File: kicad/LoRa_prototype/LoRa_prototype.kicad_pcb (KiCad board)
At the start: 2 copper layers, 145 parts, among them J1 Conn_ST_STDC14, J10 SYS, J11 BME, J12 GPS, J13 GPS_UART, J14 SPI_FLASH, J15 SYS, J18 MCO, J2 USB_C_Receptacle_PowerOnly_6P, J3 BAT, J4 SMA Female, J5 FG, J6 I2C1, J7 BQ, J8 BMV, J9 UART1, Q1 DTC143Z, Q2 DTC143Z, SW1 NRST, U1 TC1262-33, U10 STM32WL54CCUx, U2 BQ24074RGTT, U3 MAX17048, U4 SPV1050, U5 AS179-92LF, U6 L80-R, U7 BME688, U8 W25Q16JVSS, U9 BMV080, X1 LSE, X2 NT2016SF

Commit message: Routed HSE
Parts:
- removed R2: 0, Resistor_SMD:R_0603_1608Metric
- moved X2 81.9 mm to (157.7, 103.0)
- moved X1 69.2 mm to (175.2, 106.0)
- moved C9 54.2 mm to (157.8, 105.5), turned to 180 degrees
- moved C4 52.5 mm to (174.4, 104.0)
- moved C8 52.0 mm to (174.4, 108.0)
- moved C2 51.8 mm to (157.8, 100.5)
- moved C10 33.8 mm to (68.5, 155.8)
- moved C35 33.8 mm to (61.1, 154.6)
- moved C36 33.8 mm to (61.1, 157.7)
- moved C7 33.8 mm to (68.5, 154.0)
- moved J4 33.8 mm to (62.2, 148.6)
- moved C37 33.8 mm to (61.1, 160.7)
- moved L8 33.8 mm to (65.3, 154.4)
- moved U5 33.8 mm to (65.3, 160.0)
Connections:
- C7 pad 1: Net-(C7-Pad1) -> Net-(C37-Pad2)
- L8 pad 1: Net-(C7-Pad1) -> Net-(C37-Pad2)
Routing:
- net Net-(X2-OUT): track 0.00 -> 5.53 mm
- net /MCU/VDD_TCXO: track 0.00 -> 4.85 mm
- net /MCU/HSE32_IN: track 0.00 -> 3.44 mm
- net GND: track 0.00 -> 1.80 mm

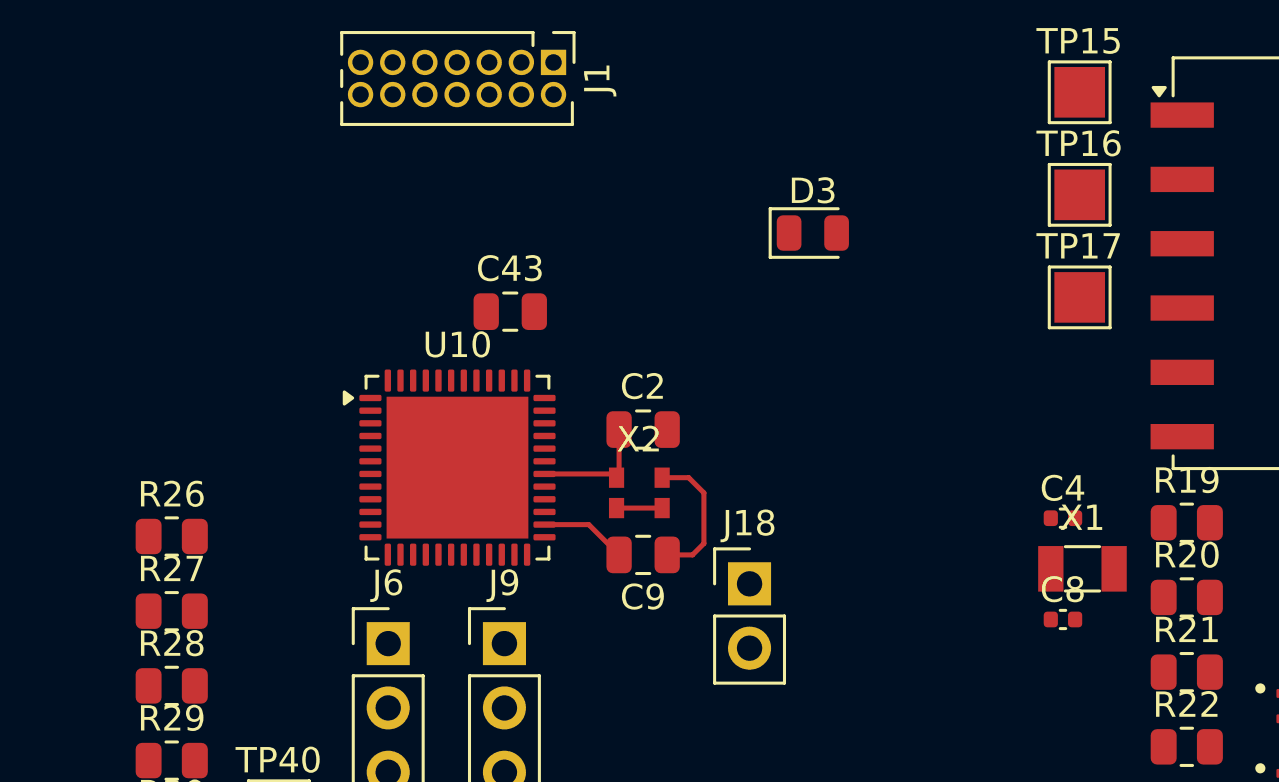
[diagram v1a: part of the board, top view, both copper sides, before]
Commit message: Routed LSE
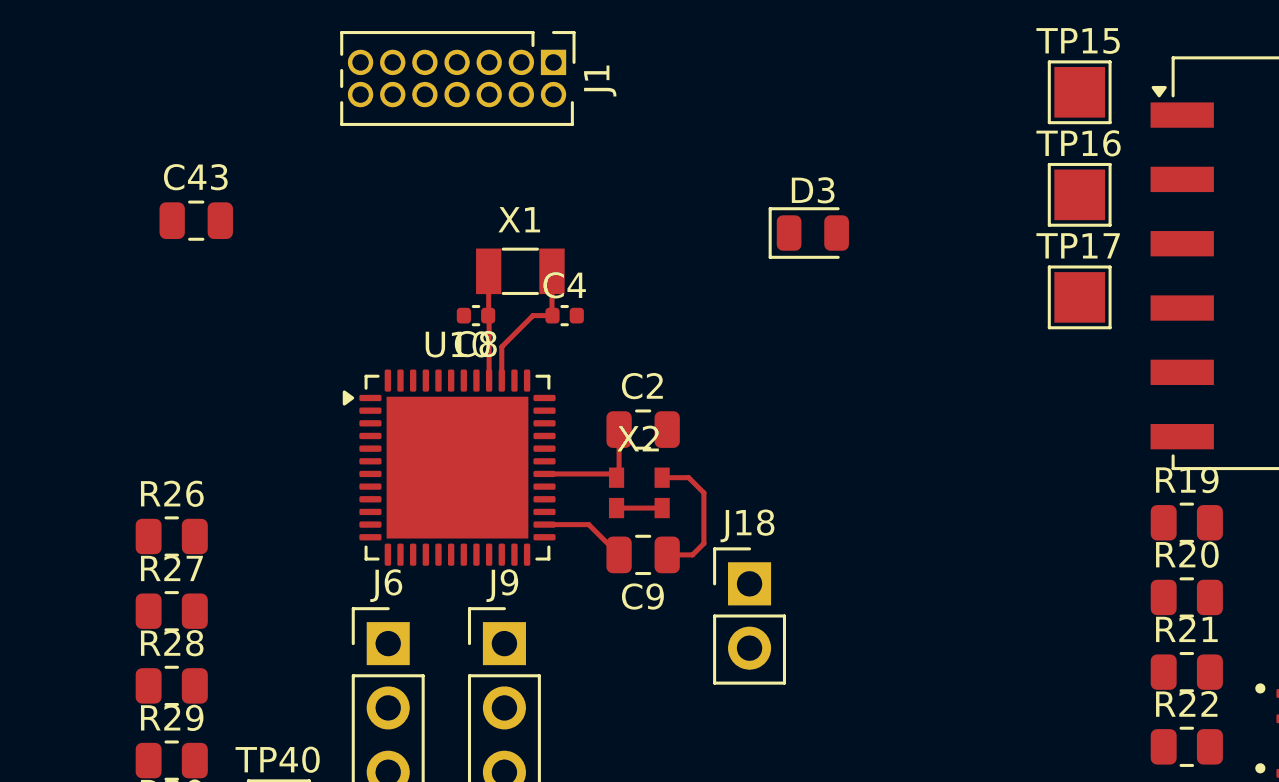
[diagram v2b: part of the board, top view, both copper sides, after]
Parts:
- moved C8 26.1 mm to (151.2, 96.0), turned to 180 degrees
- moved X1 25.1 mm to (153.0, 94.2)
- moved C4 21.2 mm to (154.8, 96.0)
- moved C43 12.9 mm to (140.2, 92.2)
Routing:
- net /MCU/OSC32_IN: track 0.00 -> 5.60 mm
- net /MCU/OSC32_OUT: track 0.00 -> 4.34 mm
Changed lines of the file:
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@@
 	(footprint "Capacitor_SMD:C_0402_1005Metric"
 		(layer "F.Cu")
-		(at 174.43 104)
+		(at 154.75 96)
 		(descr "Capacitor SMD 0402 (1005 Metric), square (rectangular) end terminal, IPC-7351 nominal, (Body size source: IPC-SM-782 page 76, https://www.pcb-3d.com/wordpress/wp-content/uploads/ipc-sm-782a_amendment_1_and_2.pdf)")
 		(tags "capacitor")
@@
 	(footprint "Capacitor_SMD:C_0402_1005Metric"
 		(layer "F.Cu")
-		(at 174.43 108)
+		(at 151.25 96 180)
 		(descr "Capacitor SMD 0402 (1005 Metric), square (rectangular) end terminal, IPC-7351 nominal, (Body size source: IPC-SM-782 page 76, https://www.pcb-3d.com/wordpress/wp-content/uploads/ipc-sm-782a_amendment_1_and_2.pdf)")
 		(tags "capacitor")
@@
 		(duplicate_pad_numbers_are_jumpers no)
 		(fp_line
-			(start -0.107836 -0.36)
-			(end 0.107836 -0.36)
+			(start -0.107836 0.36)
+			(end 0.107836 0.36)
 			(stroke
 				(width 0.12)
@@
 		)
 		(fp_line
-			(start -0.107836 0.36)
-			(end 0.107836 0.36)
+			(start -0.107836 -0.36)
+			(end 0.107836 -0.36)
 			(stroke
 				(width 0.12)
@@
 		)
 		(pad "1" smd roundrect
-			(at -0.48 0)
+			(at -0.48 0 180)
 			(size 0.56 0.62)
 			(layers "F.Cu" "F.Mask" "F.Paste")
@@
 		)
 		(pad "2" smd roundrect
-			(at 0.48 0)
+			(at 0.48 0 180)
 			(size 0.56 0.62)
 			(layers "F.Cu" "F.Mask" "F.Paste")
@@
 	(footprint "Crystal:Crystal_SMD_3215-2Pin_3.2x1.5mm"
 		(layer "F.Cu")
-		(at 175.2 106)
+		(at 153 94.25)
 		(descr "SMD Crystal FC-135 https://support.epson.biz/td/api/doc_check.php?dl=brief_FC-135R_en.pdf")
 		(tags "SMD SMT Crystal")
@@
 	(footprint "Capacitor_SMD:C_0805_2012Metric"
 		(layer "F.Cu")
-		(at 152.602031 95.842959)
+		(at 140.2 92.25)
 		(descr "Capacitor SMD 0805 (2012 Metric), square (rectangular) end terminal, IPC-7351 nominal, (Body size source: IPC-SM-782 page 76, https://www.pcb-3d.com/wordpress/wp-content/uploads/ipc-sm-782a_amendment_1_and_2.pdf, https://docs.google.com/spreadsheets/d/1BsfQQcO9C6DZCsRaXUlFlo91Tg2WpOkGARC1WS5S8t0/edit?usp=sharing)")
 		(tags "capacitor")
@@
 	)
 	(segment
+		(start 154.25 95.98)
+		(end 154.27 96)
+		(width 0.2)
+		(layer "F.Cu")
+		(net "/MCU/OSC32_IN")
+	)
+	(segment
+		(start 153.5 96)
+		(end 154.27 96)
+		(width 0.2)
+		(layer "F.Cu")
+		(net "/MCU/OSC32_IN")
+	)
+	(segment
+		(start 154.25 94.25)
+		(end 154.25 95.98)
+		(width 0.2)
+		(layer "F.Cu")
+		(net "/MCU/OSC32_IN")
+	)
+	(segment
+		(start 152.267031 98.565459)
+		(end 152.267031 97.232969)
+		(width 0.2)
+		(layer "F.Cu")
+		(net "/MCU/OSC32_IN")
+	)
+	(segment
+		(start 152.267031 97.232969)
+		(end 153.5 96)
+		(width 0.2)
+		(layer "F.Cu")
+		(net "/MCU/OSC32_IN")
+	)
+	(segment
 		(start 155.702959 104.252959)
 		(end 153.954531 104.252959)
@@
 	)
 	(segment
+		(start 151.767031 96.037031)
+		(end 151.73 96)
+		(width 0.2)
+		(layer "F.Cu")
+		(net "/MCU/OSC32_OUT")
+	)
+	(segment
+		(start 151.75 94.25)
+		(end 151.75 95.98)
+		(width 0.2)
+		(layer "F.Cu")
+		(net "/MCU/OSC32_OUT")
+	)
+	(segment
+		(start 151.767031 98.565459)
+		(end 151.767031 96.037031)
+		(width 0.2)
+		(layer "F.Cu")
+		(net "/MCU/OSC32_OUT")
+	)
+	(segment
+		(start 151.75 95.98)
+		(end 151.73 96)
+		(width 0.2)
+		(layer "F.Cu")
+		(net "/MCU/OSC32_OUT")
+	)
+	(segment
 		(start 160.25 105)
 		(end 159.8 105.45)
@@
 	)
 	(group "LSE"
-		(members "25ea31a0-66d6-4e1f-b509-5657541be55f" "4ed70896-ffde-42e4-9e79-904dfb71fc16"
-			"9a9c0433-bba5-437b-b830-2b0c35f599ee"
+		(members "25ea31a0-66d6-4e1f-b509-5657541be55f" "2998f5f7-395f-44a4-b5e5-e20377530b92"
+			"4103ce47-f324-4e95-b2e1-24609d7de2ad" "4ed70896-ffde-42e4-9e79-904dfb71fc16"
+			"62b5c70e-7bc1-46a2-bc2c-e6ab2a79eabf" "9a9c0433-bba5-437b-b830-2b0c35f599ee"
+			"9b666859-1e22-4758-9d18-4f5b0084d5c2"
 		)
 	)

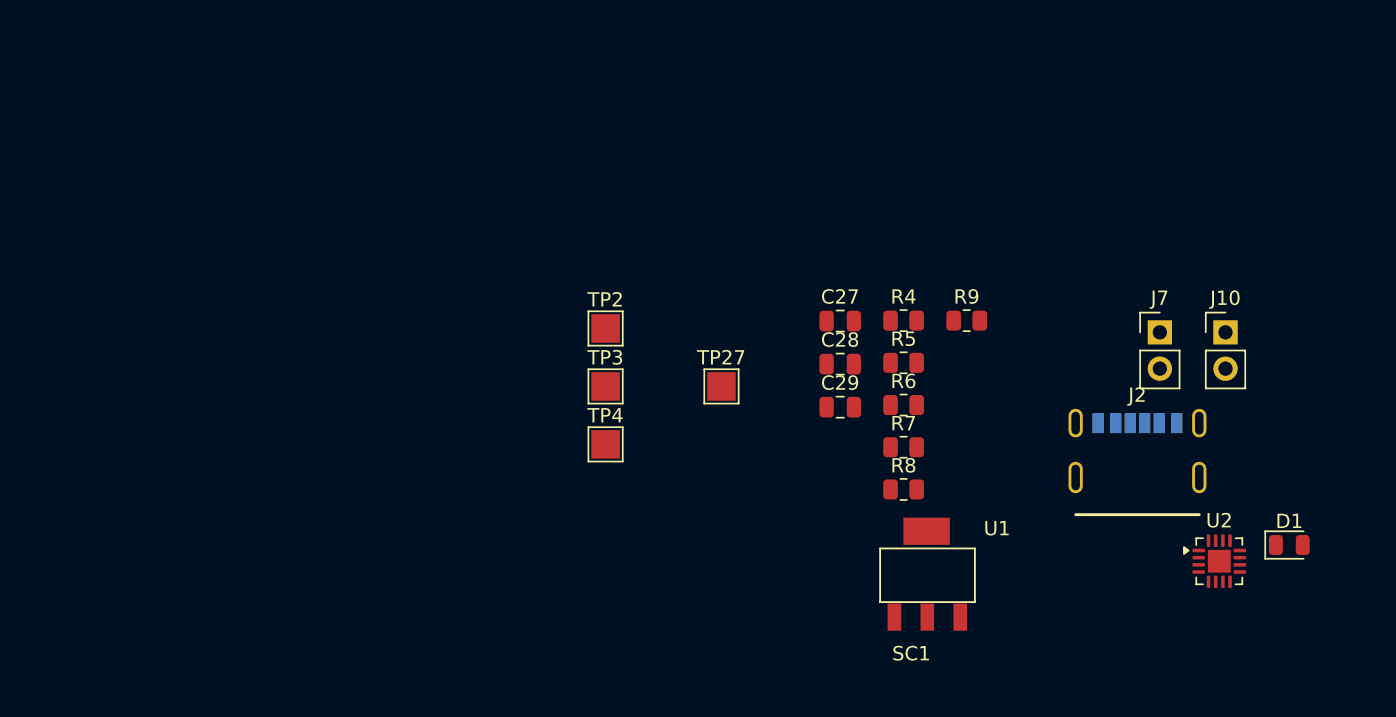
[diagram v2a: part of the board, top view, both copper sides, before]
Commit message: Routed USB and charging IC
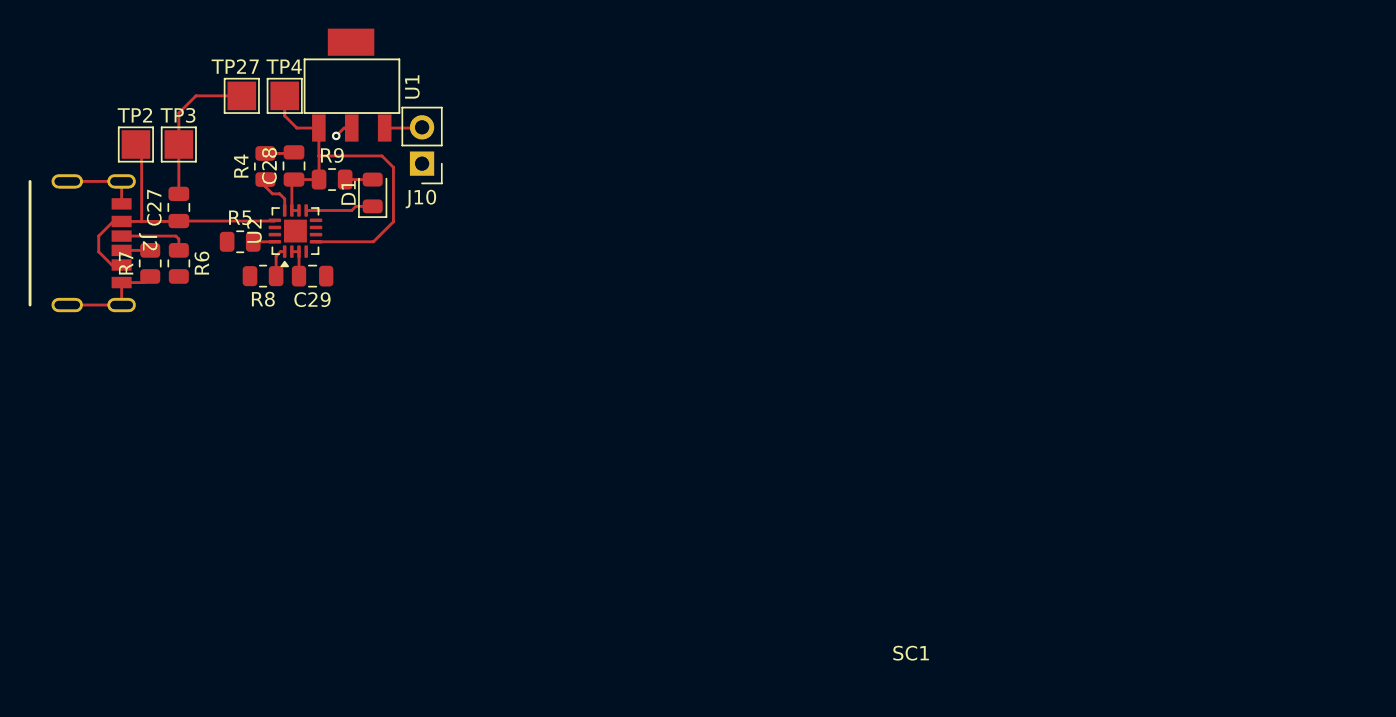
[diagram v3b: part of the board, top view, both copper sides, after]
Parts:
- removed J7: BQ, Connector_PinHeader_2.54mm:PinHeader_1x02_P2.54mm_Vertical
- moved J2 72.1 mm to (31.6, 43.9), turned to -90 degrees
- moved D1 68.6 mm to (49.1, 40.4), turned to 90 degrees
- moved U2 68.6 mm to (43.8, 43.0), turned to 90 degrees
- moved J10 57.4 mm to (52.6, 38.3), turned to 180 degrees
- moved R7 54.2 mm to (33.6, 45.3), turned to 90 degrees
- moved U1 52.8 mm to (44.9, 36.8)
- moved R6 51.6 mm to (35.6, 45.3), turned to -90 degrees
- moved R8 47.2 mm to (41.5, 46.2), turned to 180 degrees
- moved R5 47.1 mm to (39.9, 43.8)
- moved C27 46.9 mm to (35.6, 41.4), turned to 90 degrees
- moved R4 45.9 mm to (41.6, 38.5), turned to 90 degrees
- moved R9 45.4 mm to (46.3, 39.5)
- moved C28 40.6 mm to (43.6, 38.5), turned to 90 degrees
- moved TP27 39.2 mm to (40.0, 33.6), turned to 90 degrees
- moved C29 38.0 mm to (45.0, 46.2), turned to 180 degrees
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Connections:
- C27 pad 1: Net-(J7-Pin_1) -> Net-(U2-IN)
- J2 pad A9: Net-(J7-Pin_1) -> Net-(U2-IN)
- J2 pad B9: Net-(J7-Pin_1) -> Net-(U2-IN)
- TP2 pad 1: Net-(J7-Pin_1) -> Net-(U2-IN)
- U2 pad 13: Net-(J7-Pin_2) -> Net-(U2-IN)
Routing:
- net /POWER/OUT: track 0.00 -> 27.5 mm
- net GND: track 1.80 -> 28.6 mm, vias 0 -> 1
- net Net-(U2-IN): track 0.00 -> 21.4 mm
- net Net-(J2-CC1): track 0.00 -> 4.88 mm
- net Net-(D1-K): track 0.00 -> 4.77 mm
- net Net-(U2-ILIM): track 0.00 -> 3.01 mm
- net Net-(J10-Pin_2): track 0.00 -> 2.63 mm
- net /POWER/BAT+: track 0.00 -> 2.21 mm
- net Net-(U2-TS): track 0.00 -> 2.13 mm
- net Net-(J2-CC2): track 0.00 -> 2.00 mm
- net Net-(D1-A): track 0.00 -> 1.92 mm
- net Net-(U2-ISET): track 0.00 -> 1.51 mm

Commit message: Stable commit
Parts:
- moved J3 71.5 mm to (41.5, 81.2), turned to -90 degrees
- moved C33 64.8 mm to (26.1, 87.6)
- moved C34 64.2 mm to (26.2, 91.4)
- moved R18 53.3 mm to (48.7, 85.0), turned to 180 degrees
- moved U4 49.5 mm to (56.4, 87.0)
- moved R17 48.6 mm to (52.5, 85.0), turned to 180 degrees
- moved C32 39.1 mm to (54.0, 90.2)
- moved C30 38.3 mm to (51.2, 88.6), turned to 90 degrees
- moved SC1 38.2 mm to (52.2, 73.4)
- moved R11 37.4 mm to (56.6, 92.9), turned to 90 degrees
- moved R12 37.0 mm to (58.6, 92.9), turned to 90 degrees
- moved TP14 36.5 mm to (40.8, 86.8)
- moved TP34 36.5 mm to (48.6, 89.0)
- moved R13 36.3 mm to (61.9, 92.2)
- moved R15 34.4 mm to (61.9, 96.0)
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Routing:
- net /POWER/STORE: track 0.00 -> 26.9 mm, vias 0 -> 2
- net Net-(U4-UVP): track 0.00 -> 10.5 mm
- net Net-(U4-EOC): track 0.00 -> 10.1 mm
- net /POWER/MPP_SET: track 0.00 -> 6.53 mm
- net /POWER/MPP: track 0.00 -> 5.23 mm
- net /POWER/~{BATT_CONN}: track 0.00 -> 4.41 mm
- net Net-(U4-MPP_REF): track 0.00 -> 3.97 mm
- net /POWER/~{BATT_CHG}: track 0.00 -> 3.75 mm
- net GND: track 28.6 -> 31.8 mm
- net /POWER/BAT+: track 2.21 -> 4.60 mm
- net Net-(J15-Pin_2): track 0.00 -> 1.94 mm
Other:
- copper layers 2 -> 4

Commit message: Stable commit
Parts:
- moved L7 38.6 mm to (57.2, 83.6), turned to 90 degrees
- moved TP11 30.3 mm to (65.1, 84.5)
- moved TP8 26.8 mm to (65.1, 81.5)
- moved TP28 22.7 mm to (65.1, 87.5)
- moved J15 18.4 mm to (67.9, 90.8), turned to -90 degrees
- moved C34 1.61 mm to (26.1, 89.8)
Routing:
- net /POWER/STORE: track 26.9 -> 45.8 mm, vias 2 -> 4
- net /POWER/MPP: track 5.23 -> 18.9 mm
- net Net-(U4-IN_LV): track 0.00 -> 11.2 mm, vias 0 -> 2
- net GND: track 31.8 -> 36.0 mm

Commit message: Stable commit
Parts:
- moved U3 77.7 mm to (80.5, 42.5)
- moved R10 69.5 mm to (80.5, 44.8)
- moved TP29 66.1 mm to (69.5, 41.6)
- moved TP30 66.1 mm to (69.5, 45.7)
- moved TP31 66.1 mm to (69.5, 49.8)
- moved J5 66.1 mm to (95.5, 29.8)
- moved TP32 66.1 mm to (73.5, 29.5)
- moved TP5 66.1 mm to (61.4, 41.6)
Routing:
- net Net-(J15-Pin_2): track 1.94 -> 9.38 mm
- net Net-(J5-Pin_1): track 0.00 -> 4.44 mm
- net /MCU/~{ALRT}: track 0.00 -> 1.58 mm

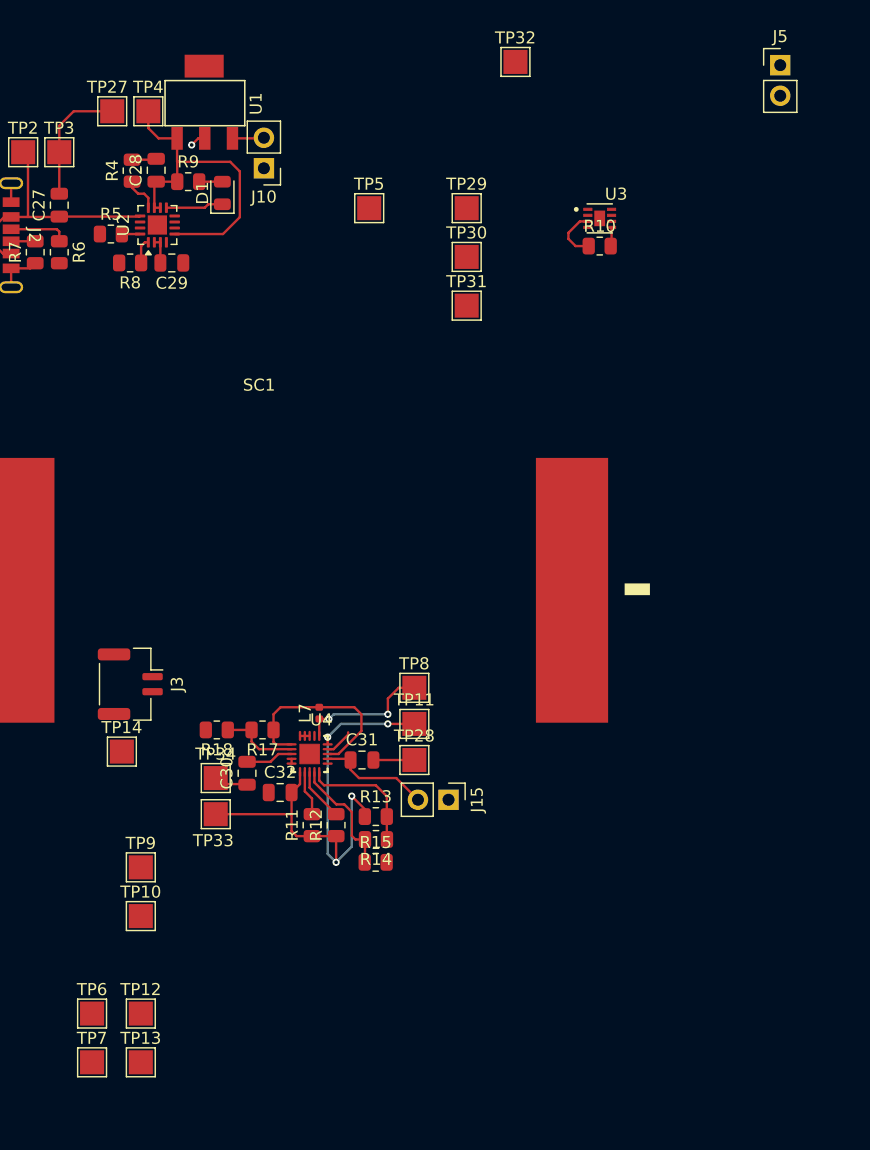
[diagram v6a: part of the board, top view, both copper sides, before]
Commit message: Done routing fuel gauge
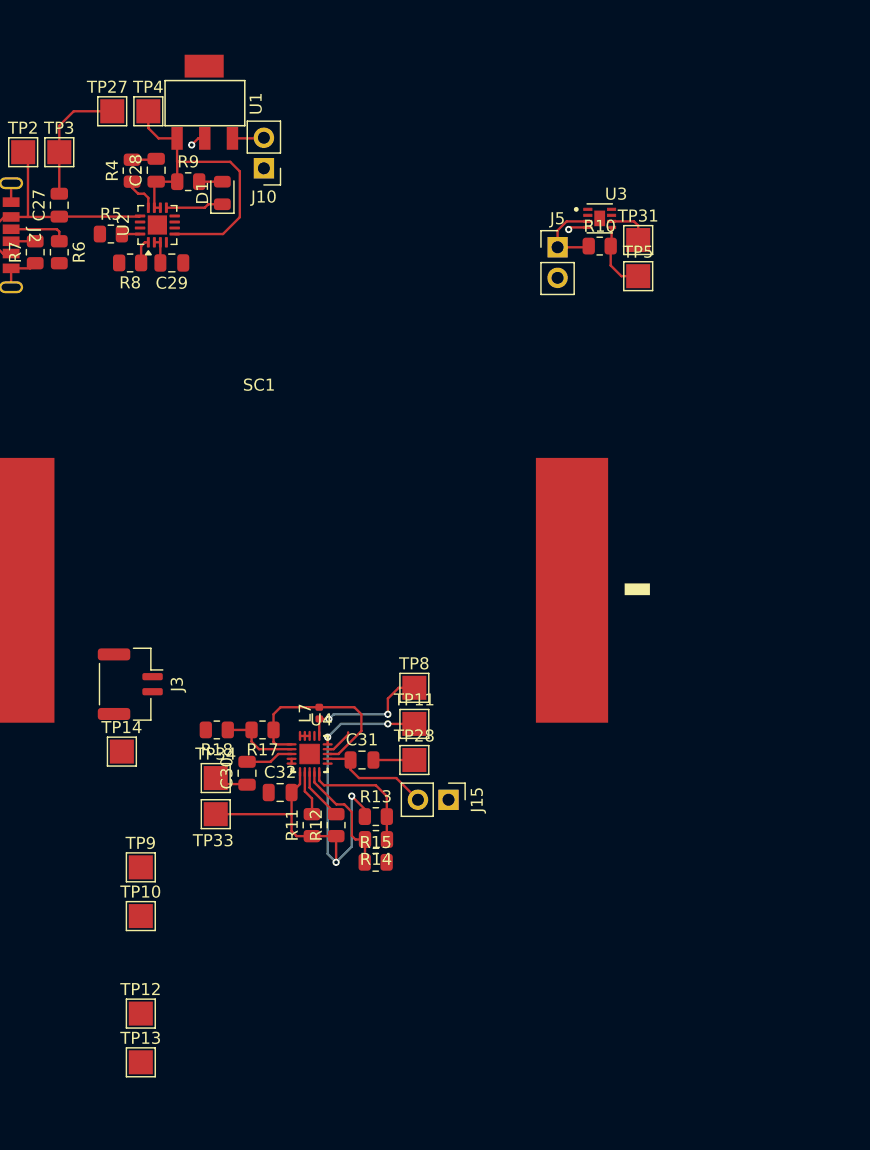
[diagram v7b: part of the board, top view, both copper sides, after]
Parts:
- removed TP29: SDA_FG, TestPoint:TestPoint_Pad_2.0x2.0mm
- removed TP30: SCL_FG, TestPoint:TestPoint_Pad_2.0x2.0mm
- removed TP32: GND, TestPoint:TestPoint_Pad_2.0x2.0mm
- removed TP6: ~{BAT_CHG}, TestPoint:TestPoint_Pad_2.0x2.0mm
- removed TP7: ~{BAT_CONN}, TestPoint:TestPoint_Pad_2.0x2.0mm
- moved J5 23.9 mm to (77.0, 44.9)
- moved TP5 23.1 mm to (83.7, 47.3)
- moved TP31 15.3 mm to (83.7, 44.3)
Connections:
- U3 pad 2: /POWER/BAT+ -> unconnected-(U3-CELL-Pad2)
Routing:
- net GND: track 36.0 -> 41.3 mm, vias 1 -> 2
- net /MCU/~{ALRT}: track 1.58 -> 5.85 mm
- net Net-(J5-Pin_1): track 4.44 -> 6.85 mm
